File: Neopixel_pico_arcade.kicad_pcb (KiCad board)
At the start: 4 copper layers, 100 x 100 mm, 0 parts

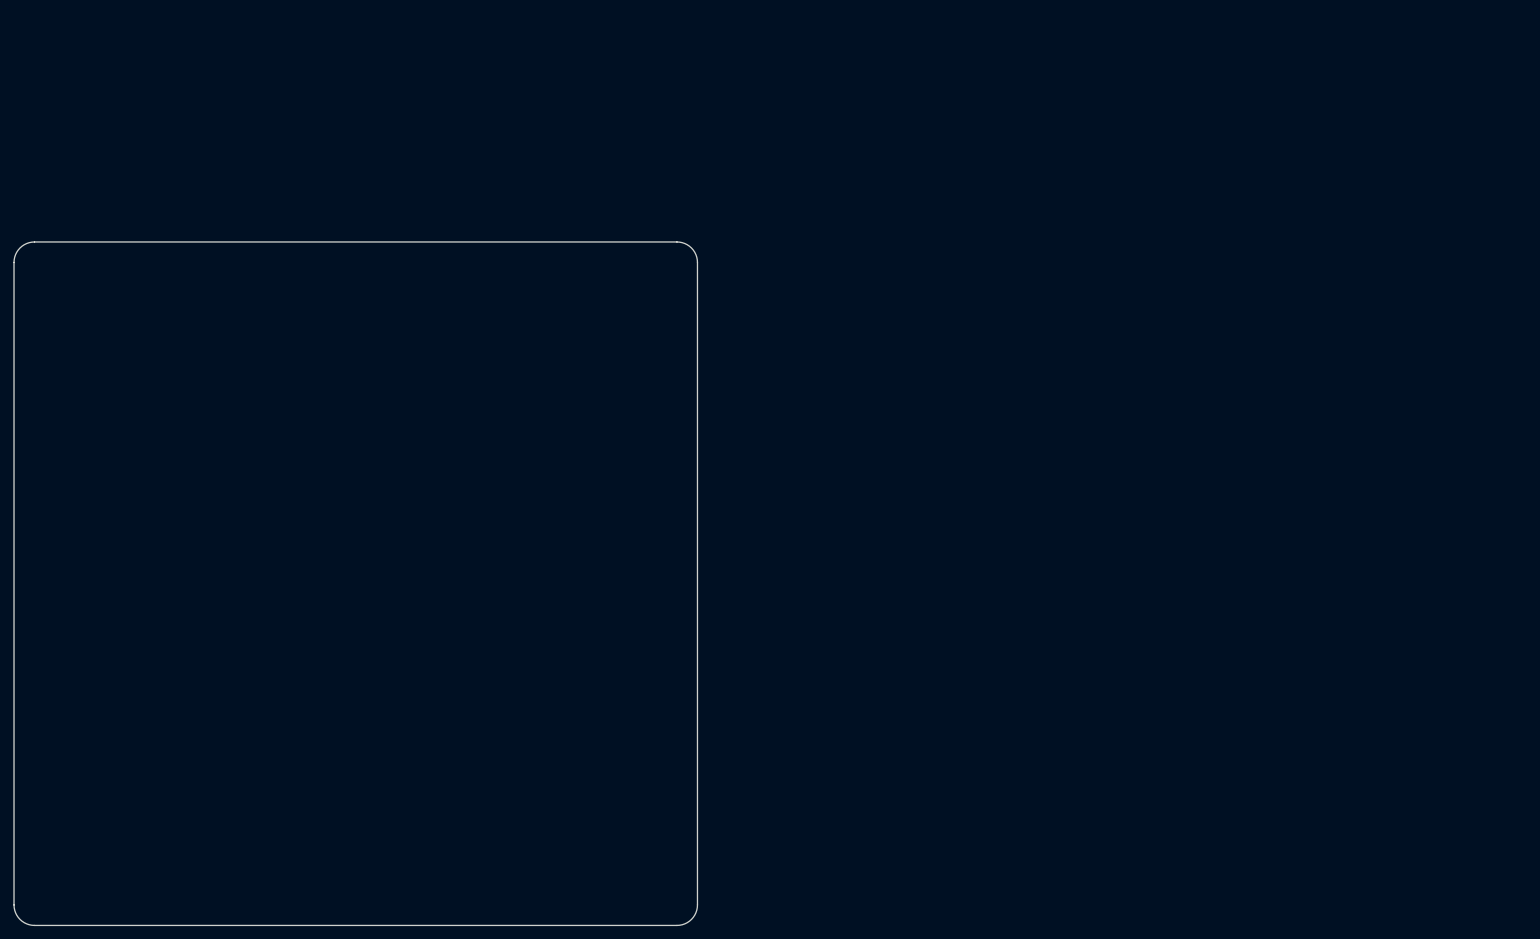
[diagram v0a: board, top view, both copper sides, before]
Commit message: Moves bottom side components roughly into place
The NES connector will still need to move to make space for the LEDs.
This probably means the PCB will need to grow.
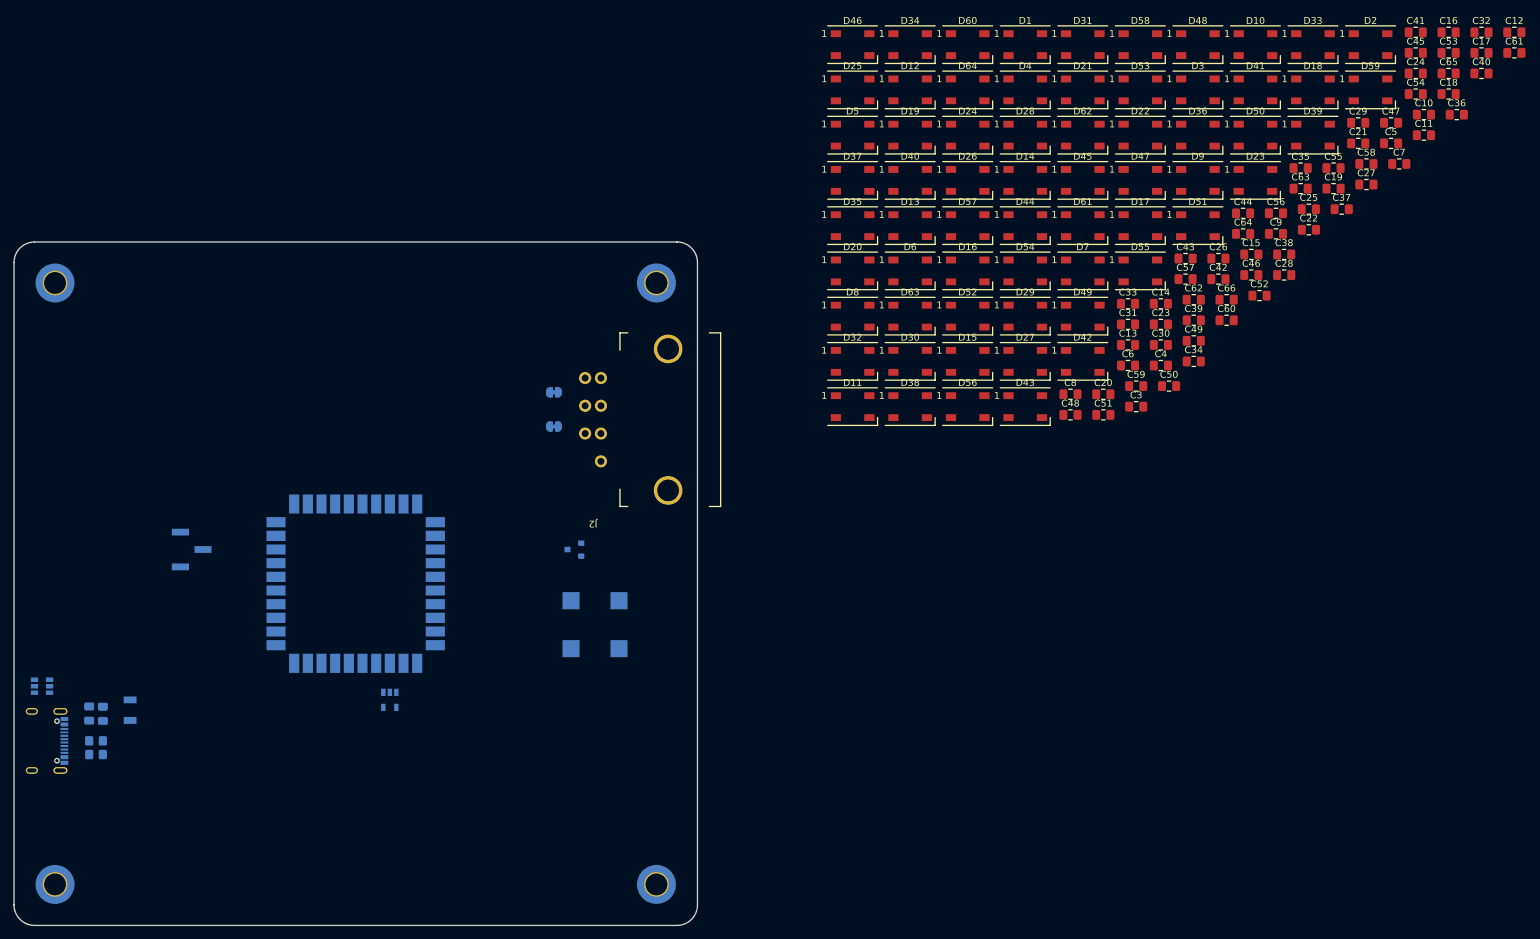
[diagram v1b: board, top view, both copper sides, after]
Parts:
- added BZ1: Buzzer, Buzzer_Beeper:MagneticBuzzer_CUI_CMT-8504-100-SMT, B.Cu at (185.0, 106.0)
- added C1: 4.7µF, Capacitor_SMD:C_0805_2012Metric_Pad1.18x1.45mm_HandSolder, B.Cu at (113.0, 119.0)
- added C10: 100nF, Capacitor_SMD:C_0805_2012Metric_Pad1.18x1.45mm_HandSolder, F.Cu at (306.3, 31.4)
- added C11: 100nF, Capacitor_SMD:C_0805_2012Metric_Pad1.18x1.45mm_HandSolder, F.Cu at (306.3, 34.4)
- added C12: 100nF, Capacitor_SMD:C_0805_2012Metric_Pad1.18x1.45mm_HandSolder, F.Cu at (319.5, 19.3)
- added C13: 100nF, Capacitor_SMD:C_0805_2012Metric_Pad1.18x1.45mm_HandSolder, F.Cu at (263.0, 65.1)
- added C14: 100nF, Capacitor_SMD:C_0805_2012Metric_Pad1.18x1.45mm_HandSolder, F.Cu at (267.8, 59.0)
- added C15: 100nF, Capacitor_SMD:C_0805_2012Metric_Pad1.18x1.45mm_HandSolder, F.Cu at (281.0, 51.8)
- added C16: 100nF, Capacitor_SMD:C_0805_2012Metric_Pad1.18x1.45mm_HandSolder, F.Cu at (309.9, 19.3)
- added C17: 100nF, Capacitor_SMD:C_0805_2012Metric_Pad1.18x1.45mm_HandSolder, F.Cu at (314.7, 22.3)
- added C18: 100nF, Capacitor_SMD:C_0805_2012Metric_Pad1.18x1.45mm_HandSolder, F.Cu at (309.9, 28.4)
- added C19: 100nF, Capacitor_SMD:C_0805_2012Metric_Pad1.18x1.45mm_HandSolder, F.Cu at (293.1, 42.2)
- added C2: 100nF, Capacitor_SMD:C_0805_2012Metric_Pad1.18x1.45mm_HandSolder, B.Cu at (111.0, 119.0)
- added C20: 100nF, Capacitor_SMD:C_0805_2012Metric_Pad1.18x1.45mm_HandSolder, F.Cu at (259.4, 72.3)
- added C21: 100nF, Capacitor_SMD:C_0805_2012Metric_Pad1.18x1.45mm_HandSolder, F.Cu at (296.7, 35.6)
- added C22: 100nF, Capacitor_SMD:C_0805_2012Metric_Pad1.18x1.45mm_HandSolder, F.Cu at (289.5, 48.2)
- added C23: 100nF, Capacitor_SMD:C_0805_2012Metric_Pad1.18x1.45mm_HandSolder, F.Cu at (267.8, 62.1)
- added C24: 100nF, Capacitor_SMD:C_0805_2012Metric_Pad1.18x1.45mm_HandSolder, F.Cu at (305.1, 25.3)
- added C25: 100nF, Capacitor_SMD:C_0805_2012Metric_Pad1.18x1.45mm_HandSolder, F.Cu at (289.5, 45.2)
- added C26: 100nF, Capacitor_SMD:C_0805_2012Metric_Pad1.18x1.45mm_HandSolder, F.Cu at (276.2, 52.4)
- added C27: 100nF, Capacitor_SMD:C_0805_2012Metric_Pad1.18x1.45mm_HandSolder, F.Cu at (297.9, 41.6)
- added C28: 100nF, Capacitor_SMD:C_0805_2012Metric_Pad1.18x1.45mm_HandSolder, F.Cu at (285.8, 54.8)
- added C29: 100nF, Capacitor_SMD:C_0805_2012Metric_Pad1.18x1.45mm_HandSolder, F.Cu at (296.7, 32.6)
- added C3: 100nF, Capacitor_SMD:C_0805_2012Metric_Pad1.18x1.45mm_HandSolder, F.Cu at (264.2, 74.1)
- added C30: 100nF, Capacitor_SMD:C_0805_2012Metric_Pad1.18x1.45mm_HandSolder, F.Cu at (267.8, 65.1)
- added C31: 100nF, Capacitor_SMD:C_0805_2012Metric_Pad1.18x1.45mm_HandSolder, F.Cu at (263.0, 62.1)
- added C32: 100nF, Capacitor_SMD:C_0805_2012Metric_Pad1.18x1.45mm_HandSolder, F.Cu at (314.7, 19.3)
- added C33: 100nF, Capacitor_SMD:C_0805_2012Metric_Pad1.18x1.45mm_HandSolder, F.Cu at (263.0, 59.0)
- added C34: 100nF, Capacitor_SMD:C_0805_2012Metric_Pad1.18x1.45mm_HandSolder, F.Cu at (272.6, 67.5)
- added C35: 100nF, Capacitor_SMD:C_0805_2012Metric_Pad1.18x1.45mm_HandSolder, F.Cu at (288.3, 39.2)
- added C36: 100nF, Capacitor_SMD:C_0805_2012Metric_Pad1.18x1.45mm_HandSolder, F.Cu at (311.1, 31.4)
- added C37: 100nF, Capacitor_SMD:C_0805_2012Metric_Pad1.18x1.45mm_HandSolder, F.Cu at (294.3, 45.2)
- added C38: 100nF, Capacitor_SMD:C_0805_2012Metric_Pad1.18x1.45mm_HandSolder, F.Cu at (285.8, 51.8)
- added C39: 100nF, Capacitor_SMD:C_0805_2012Metric_Pad1.18x1.45mm_HandSolder, F.Cu at (272.6, 61.5)
- added C4: 100nF, Capacitor_SMD:C_0805_2012Metric_Pad1.18x1.45mm_HandSolder, F.Cu at (267.8, 68.1)
- added C40: 100nF, Capacitor_SMD:C_0805_2012Metric_Pad1.18x1.45mm_HandSolder, F.Cu at (314.7, 25.3)
- added C41: 100nF, Capacitor_SMD:C_0805_2012Metric_Pad1.18x1.45mm_HandSolder, F.Cu at (305.1, 19.3)
- added C42: 100nF, Capacitor_SMD:C_0805_2012Metric_Pad1.18x1.45mm_HandSolder, F.Cu at (276.2, 55.4)
- added C43: 100nF, Capacitor_SMD:C_0805_2012Metric_Pad1.18x1.45mm_HandSolder, F.Cu at (271.4, 52.4)
- added C44: 100nF, Capacitor_SMD:C_0805_2012Metric_Pad1.18x1.45mm_HandSolder, F.Cu at (279.8, 45.8)
- added C45: 100nF, Capacitor_SMD:C_0805_2012Metric_Pad1.18x1.45mm_HandSolder, F.Cu at (305.1, 22.3)
- added C46: 100nF, Capacitor_SMD:C_0805_2012Metric_Pad1.18x1.45mm_HandSolder, F.Cu at (281.0, 54.8)
- added C47: 100nF, Capacitor_SMD:C_0805_2012Metric_Pad1.18x1.45mm_HandSolder, F.Cu at (301.5, 32.6)
- added C48: 100nF, Capacitor_SMD:C_0805_2012Metric_Pad1.18x1.45mm_HandSolder, F.Cu at (254.6, 75.3)
- added C49: 100nF, Capacitor_SMD:C_0805_2012Metric_Pad1.18x1.45mm_HandSolder, F.Cu at (272.6, 64.5)
- added C5: 100nF, Capacitor_SMD:C_0805_2012Metric_Pad1.18x1.45mm_HandSolder, F.Cu at (301.5, 35.6)
- added C50: 100nF, Capacitor_SMD:C_0805_2012Metric_Pad1.18x1.45mm_HandSolder, F.Cu at (269.0, 71.1)
- added C51: 100nF, Capacitor_SMD:C_0805_2012Metric_Pad1.18x1.45mm_HandSolder, F.Cu at (259.4, 75.3)
- added C52: 100nF, Capacitor_SMD:C_0805_2012Metric_Pad1.18x1.45mm_HandSolder, F.Cu at (282.2, 57.8)
- added C53: 100nF, Capacitor_SMD:C_0805_2012Metric_Pad1.18x1.45mm_HandSolder, F.Cu at (309.9, 22.3)
- added C54: 100nF, Capacitor_SMD:C_0805_2012Metric_Pad1.18x1.45mm_HandSolder, F.Cu at (305.1, 28.4)
- added C55: 100nF, Capacitor_SMD:C_0805_2012Metric_Pad1.18x1.45mm_HandSolder, F.Cu at (293.1, 39.2)
- added C56: 100nF, Capacitor_SMD:C_0805_2012Metric_Pad1.18x1.45mm_HandSolder, F.Cu at (284.6, 45.8)
- added C57: 100nF, Capacitor_SMD:C_0805_2012Metric_Pad1.18x1.45mm_HandSolder, F.Cu at (271.4, 55.4)
- added C58: 100nF, Capacitor_SMD:C_0805_2012Metric_Pad1.18x1.45mm_HandSolder, F.Cu at (297.9, 38.6)
- added C59: 100nF, Capacitor_SMD:C_0805_2012Metric_Pad1.18x1.45mm_HandSolder, F.Cu at (264.2, 71.1)
- added C6: 100nF, Capacitor_SMD:C_0805_2012Metric_Pad1.18x1.45mm_HandSolder, F.Cu at (263.0, 68.1)
- added C60: 100nF, Capacitor_SMD:C_0805_2012Metric_Pad1.18x1.45mm_HandSolder, F.Cu at (277.4, 61.5)
- added C61: 100nF, Capacitor_SMD:C_0805_2012Metric_Pad1.18x1.45mm_HandSolder, F.Cu at (319.5, 22.3)
- added C62: 100nF, Capacitor_SMD:C_0805_2012Metric_Pad1.18x1.45mm_HandSolder, F.Cu at (272.6, 58.4)
- added C63: 100nF, Capacitor_SMD:C_0805_2012Metric_Pad1.18x1.45mm_HandSolder, F.Cu at (288.3, 42.2)
- added C64: 100nF, Capacitor_SMD:C_0805_2012Metric_Pad1.18x1.45mm_HandSolder, F.Cu at (279.8, 48.8)
- added C65: 100nF, Capacitor_SMD:C_0805_2012Metric_Pad1.18x1.45mm_HandSolder, F.Cu at (309.9, 25.3)
- added C66: 100nF, Capacitor_SMD:C_0805_2012Metric_Pad1.18x1.45mm_HandSolder, F.Cu at (277.4, 58.4)
- added C7: 100nF, Capacitor_SMD:C_0805_2012Metric_Pad1.18x1.45mm_HandSolder, F.Cu at (302.7, 38.6)
- added C8: 100nF, Capacitor_SMD:C_0805_2012Metric_Pad1.18x1.45mm_HandSolder, F.Cu at (254.6, 72.3)
- added C9: 100nF, Capacitor_SMD:C_0805_2012Metric_Pad1.18x1.45mm_HandSolder, F.Cu at (284.6, 48.8)
- added D1: WS2812C, LED_SMD:LED_WS2812B_PLCC4_5.0x5.0mm_P3.2mm, F.Cu at (248.0, 21.1)
- added D10: WS2812C, LED_SMD:LED_WS2812B_PLCC4_5.0x5.0mm_P3.2mm, F.Cu at (281.6, 21.1)
- added D11: WS2812C, LED_SMD:LED_WS2812B_PLCC4_5.0x5.0mm_P3.2mm, F.Cu at (222.7, 74.1)
- added D12: WS2812C, LED_SMD:LED_WS2812B_PLCC4_5.0x5.0mm_P3.2mm, F.Cu at (231.1, 27.8)
- added D13: WS2812C, LED_SMD:LED_WS2812B_PLCC4_5.0x5.0mm_P3.2mm, F.Cu at (231.1, 47.6)
- added D14: WS2812C, LED_SMD:LED_WS2812B_PLCC4_5.0x5.0mm_P3.2mm, F.Cu at (248.0, 41.0)
- added D15: WS2812C, LED_SMD:LED_WS2812B_PLCC4_5.0x5.0mm_P3.2mm, F.Cu at (239.5, 67.5)
- added D16: WS2812C, LED_SMD:LED_WS2812B_PLCC4_5.0x5.0mm_P3.2mm, F.Cu at (239.5, 54.2)
- added D17: WS2812C, LED_SMD:LED_WS2812B_PLCC4_5.0x5.0mm_P3.2mm, F.Cu at (264.8, 47.6)
- added D18: WS2812C, LED_SMD:LED_WS2812B_PLCC4_5.0x5.0mm_P3.2mm, F.Cu at (290.1, 27.8)
- added D19: WS2812C, LED_SMD:LED_WS2812B_PLCC4_5.0x5.0mm_P3.2mm, F.Cu at (231.1, 34.4)
- added D2: WS2812C, LED_SMD:LED_WS2812B_PLCC4_5.0x5.0mm_P3.2mm, F.Cu at (298.5, 21.1)
- added D20: WS2812C, LED_SMD:LED_WS2812B_PLCC4_5.0x5.0mm_P3.2mm, F.Cu at (222.7, 54.2)
- added D21: WS2812C, LED_SMD:LED_WS2812B_PLCC4_5.0x5.0mm_P3.2mm, F.Cu at (256.4, 27.8)
- added D22: WS2812C, LED_SMD:LED_WS2812B_PLCC4_5.0x5.0mm_P3.2mm, F.Cu at (264.8, 34.4)
- added D23: WS2812C, LED_SMD:LED_WS2812B_PLCC4_5.0x5.0mm_P3.2mm, F.Cu at (281.6, 41.0)
- added D24: WS2812C, LED_SMD:LED_WS2812B_PLCC4_5.0x5.0mm_P3.2mm, F.Cu at (239.5, 34.4)
- added D25: WS2812C, LED_SMD:LED_WS2812B_PLCC4_5.0x5.0mm_P3.2mm, F.Cu at (222.7, 27.8)
- added D26: WS2812C, LED_SMD:LED_WS2812B_PLCC4_5.0x5.0mm_P3.2mm, F.Cu at (239.5, 41.0)
- added D27: WS2812C, LED_SMD:LED_WS2812B_PLCC4_5.0x5.0mm_P3.2mm, F.Cu at (248.0, 67.5)
- added D28: WS2812C, LED_SMD:LED_WS2812B_PLCC4_5.0x5.0mm_P3.2mm, F.Cu at (248.0, 34.4)
- added D29: WS2812C, LED_SMD:LED_WS2812B_PLCC4_5.0x5.0mm_P3.2mm, F.Cu at (248.0, 60.9)
- added D3: WS2812C, LED_SMD:LED_WS2812B_PLCC4_5.0x5.0mm_P3.2mm, F.Cu at (273.2, 27.8)
- added D30: WS2812C, LED_SMD:LED_WS2812B_PLCC4_5.0x5.0mm_P3.2mm, F.Cu at (231.1, 67.5)
- added D31: WS2812C, LED_SMD:LED_WS2812B_PLCC4_5.0x5.0mm_P3.2mm, F.Cu at (256.4, 21.1)
- added D32: WS2812C, LED_SMD:LED_WS2812B_PLCC4_5.0x5.0mm_P3.2mm, F.Cu at (222.7, 67.5)
- added D33: WS2812C, LED_SMD:LED_WS2812B_PLCC4_5.0x5.0mm_P3.2mm, F.Cu at (290.1, 21.1)
- added D34: WS2812C, LED_SMD:LED_WS2812B_PLCC4_5.0x5.0mm_P3.2mm, F.Cu at (231.1, 21.1)
- added D35: WS2812C, LED_SMD:LED_WS2812B_PLCC4_5.0x5.0mm_P3.2mm, F.Cu at (222.7, 47.6)
- added D36: WS2812C, LED_SMD:LED_WS2812B_PLCC4_5.0x5.0mm_P3.2mm, F.Cu at (273.2, 34.4)
- added D37: WS2812C, LED_SMD:LED_WS2812B_PLCC4_5.0x5.0mm_P3.2mm, F.Cu at (222.7, 41.0)
- added D38: WS2812C, LED_SMD:LED_WS2812B_PLCC4_5.0x5.0mm_P3.2mm, F.Cu at (231.1, 74.1)
- added D39: WS2812C, LED_SMD:LED_WS2812B_PLCC4_5.0x5.0mm_P3.2mm, F.Cu at (290.1, 34.4)
- added D4: WS2812C, LED_SMD:LED_WS2812B_PLCC4_5.0x5.0mm_P3.2mm, F.Cu at (248.0, 27.8)
- added D40: WS2812C, LED_SMD:LED_WS2812B_PLCC4_5.0x5.0mm_P3.2mm, F.Cu at (231.1, 41.0)
- added D41: WS2812C, LED_SMD:LED_WS2812B_PLCC4_5.0x5.0mm_P3.2mm, F.Cu at (281.6, 27.8)
- added D42: WS2812C, LED_SMD:LED_WS2812B_PLCC4_5.0x5.0mm_P3.2mm, F.Cu at (256.4, 67.5)
- added D43: WS2812C, LED_SMD:LED_WS2812B_PLCC4_5.0x5.0mm_P3.2mm, F.Cu at (248.0, 74.1)
- added D44: WS2812C, LED_SMD:LED_WS2812B_PLCC4_5.0x5.0mm_P3.2mm, F.Cu at (248.0, 47.6)
- added D45: WS2812C, LED_SMD:LED_WS2812B_PLCC4_5.0x5.0mm_P3.2mm, F.Cu at (256.4, 41.0)
- added D46: WS2812C, LED_SMD:LED_WS2812B_PLCC4_5.0x5.0mm_P3.2mm, F.Cu at (222.7, 21.1)
- added D47: WS2812C, LED_SMD:LED_WS2812B_PLCC4_5.0x5.0mm_P3.2mm, F.Cu at (264.8, 41.0)
- added D48: WS2812C, LED_SMD:LED_WS2812B_PLCC4_5.0x5.0mm_P3.2mm, F.Cu at (273.2, 21.1)
- added D49: WS2812C, LED_SMD:LED_WS2812B_PLCC4_5.0x5.0mm_P3.2mm, F.Cu at (256.4, 60.9)
- added D5: WS2812C, LED_SMD:LED_WS2812B_PLCC4_5.0x5.0mm_P3.2mm, F.Cu at (222.7, 34.4)
- added D50: WS2812C, LED_SMD:LED_WS2812B_PLCC4_5.0x5.0mm_P3.2mm, F.Cu at (281.6, 34.4)
- added D51: WS2812C, LED_SMD:LED_WS2812B_PLCC4_5.0x5.0mm_P3.2mm, F.Cu at (273.2, 47.6)
- added D52: WS2812C, LED_SMD:LED_WS2812B_PLCC4_5.0x5.0mm_P3.2mm, F.Cu at (239.5, 60.9)
- added D53: WS2812C, LED_SMD:LED_WS2812B_PLCC4_5.0x5.0mm_P3.2mm, F.Cu at (264.8, 27.8)
- added D54: WS2812C, LED_SMD:LED_WS2812B_PLCC4_5.0x5.0mm_P3.2mm, F.Cu at (248.0, 54.2)
- added D55: WS2812C, LED_SMD:LED_WS2812B_PLCC4_5.0x5.0mm_P3.2mm, F.Cu at (264.8, 54.2)
- added D56: WS2812C, LED_SMD:LED_WS2812B_PLCC4_5.0x5.0mm_P3.2mm, F.Cu at (239.5, 74.1)
- added D57: WS2812C, LED_SMD:LED_WS2812B_PLCC4_5.0x5.0mm_P3.2mm, F.Cu at (239.5, 47.6)
- added D58: WS2812C, LED_SMD:LED_WS2812B_PLCC4_5.0x5.0mm_P3.2mm, F.Cu at (264.8, 21.1)
- added D59: WS2812C, LED_SMD:LED_WS2812B_PLCC4_5.0x5.0mm_P3.2mm, F.Cu at (298.5, 27.8)
- added D6: WS2812C, LED_SMD:LED_WS2812B_PLCC4_5.0x5.0mm_P3.2mm, F.Cu at (231.1, 54.2)
- added D60: WS2812C, LED_SMD:LED_WS2812B_PLCC4_5.0x5.0mm_P3.2mm, F.Cu at (239.5, 21.1)
- added D61: WS2812C, LED_SMD:LED_WS2812B_PLCC4_5.0x5.0mm_P3.2mm, F.Cu at (256.4, 47.6)
- added D62: WS2812C, LED_SMD:LED_WS2812B_PLCC4_5.0x5.0mm_P3.2mm, F.Cu at (256.4, 34.4)
- added D63: WS2812C, LED_SMD:LED_WS2812B_PLCC4_5.0x5.0mm_P3.2mm, F.Cu at (231.1, 60.9)
- added D64: WS2812C, LED_SMD:LED_WS2812B_PLCC4_5.0x5.0mm_P3.2mm, F.Cu at (239.5, 27.8)
- added D7: WS2812C, LED_SMD:LED_WS2812B_PLCC4_5.0x5.0mm_P3.2mm, F.Cu at (256.4, 54.2)
- added D8: WS2812C, LED_SMD:LED_WS2812B_PLCC4_5.0x5.0mm_P3.2mm, F.Cu at (222.7, 60.9)
- added D9: WS2812C, LED_SMD:LED_WS2812B_PLCC4_5.0x5.0mm_P3.2mm, F.Cu at (273.2, 41.0)
- added F1: PTC 1A, Neopixel_pico_arcade:Belfuse_0ZCJ, B.Cu at (117.0, 118.5)
- added H1: MountingHole_Pad, MountingHole:MountingHole_3.2mm_M3_ISO7380_Pad_TopOnly, B.Cu at (194.0, 56.0)
- added H2: MountingHole_Pad, MountingHole:MountingHole_3.2mm_M3_ISO7380_Pad_TopOnly, B.Cu at (106.0, 56.0)
- added H3: MountingHole_Pad, MountingHole:MountingHole_3.2mm_M3_ISO7380_Pad_TopOnly, B.Cu at (194.0, 144.0)
- added H4: MountingHole_Pad, MountingHole:MountingHole_3.2mm_M3_ISO7380_Pad_TopOnly, B.Cu at (106.0, 144.0)
- added J1: SWD_connector, Connector_PinHeader_2.54mm:PinHeader_1x03_P2.54mm_Vertical_SMD_Pin1Left, B.Cu at (126.0, 95.0)
- added J2: NES_controller_connector, Neopixel_pico_arcade:NES_Controller_connector, F.Cu at (184.7, 76.0)
- added J3: USB_C_Receptacle_USB2.0, Neopixel_pico_arcade:USB_C_Receptacle_USB_2_GTC_USB4105, B.Cu at (105.0, 123.0)
- added JP1: jmp, Jumper:SolderJumper-2_P1.3mm_Bridged_RoundedPad1.0x1.5mm, B.Cu at (179.0, 77.0)
- added JP2: jmp, Jumper:SolderJumper-2_P1.3mm_Bridged_RoundedPad1.0x1.5mm, B.Cu at (179.0, 72.0)
- added Q1: 2N7002, Package_TO_SOT_SMD:SOT-23, B.Cu at (182.0, 95.0)
- added R1: 5.1kΩ, Resistor_SMD:R_0805_2012Metric_Pad1.20x1.40mm_HandSolder, B.Cu at (112.0, 125.0)
- added R2: 5.1kΩ, Resistor_SMD:R_0805_2012Metric_Pad1.20x1.40mm_HandSolder, B.Cu at (112.0, 123.0)
- added U1: RP2040_Stamp, RP2040_stamp:RP2040_Stamp_SMD, B.Cu at (150.0, 100.0)
- added U2: SN74LV1T34DBV, Package_TO_SOT_SMD:SOT-23-5, B.Cu at (155.0, 117.0)
- added U3: SRV05-4HTG-D, Package_TO_SOT_SMD:SOT-23-6, B.Cu at (104.1, 115.0)

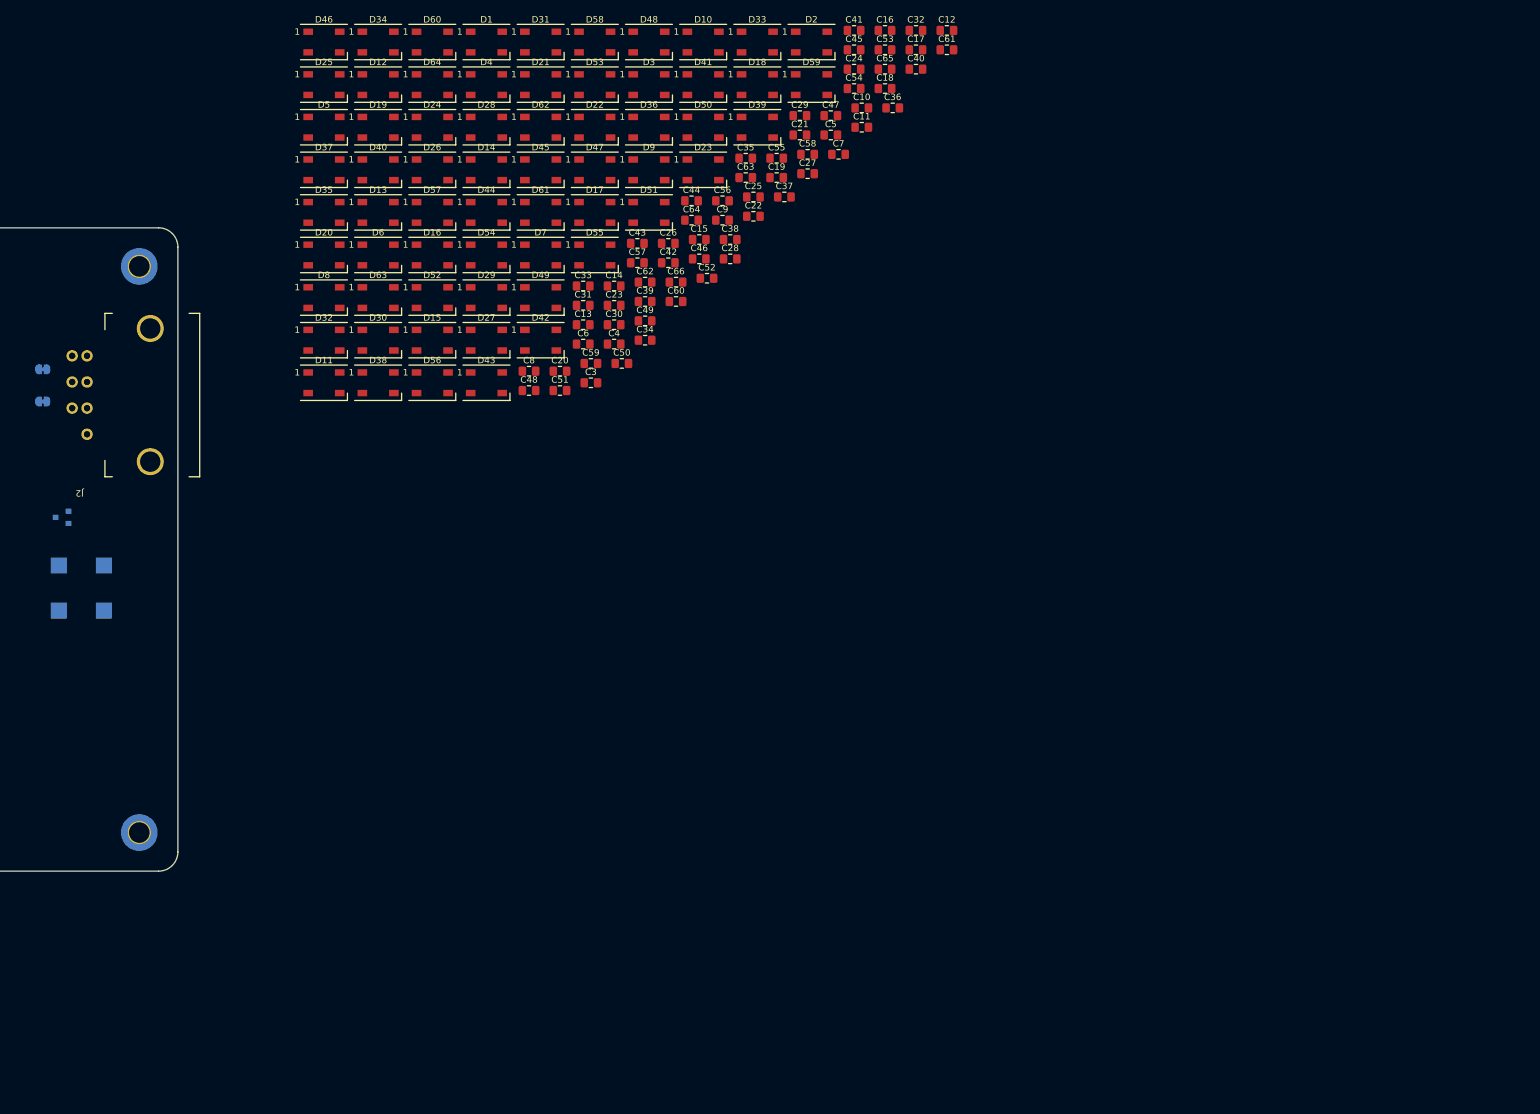
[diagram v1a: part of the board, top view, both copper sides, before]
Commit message: Arranges LEDs in an ordered matrix
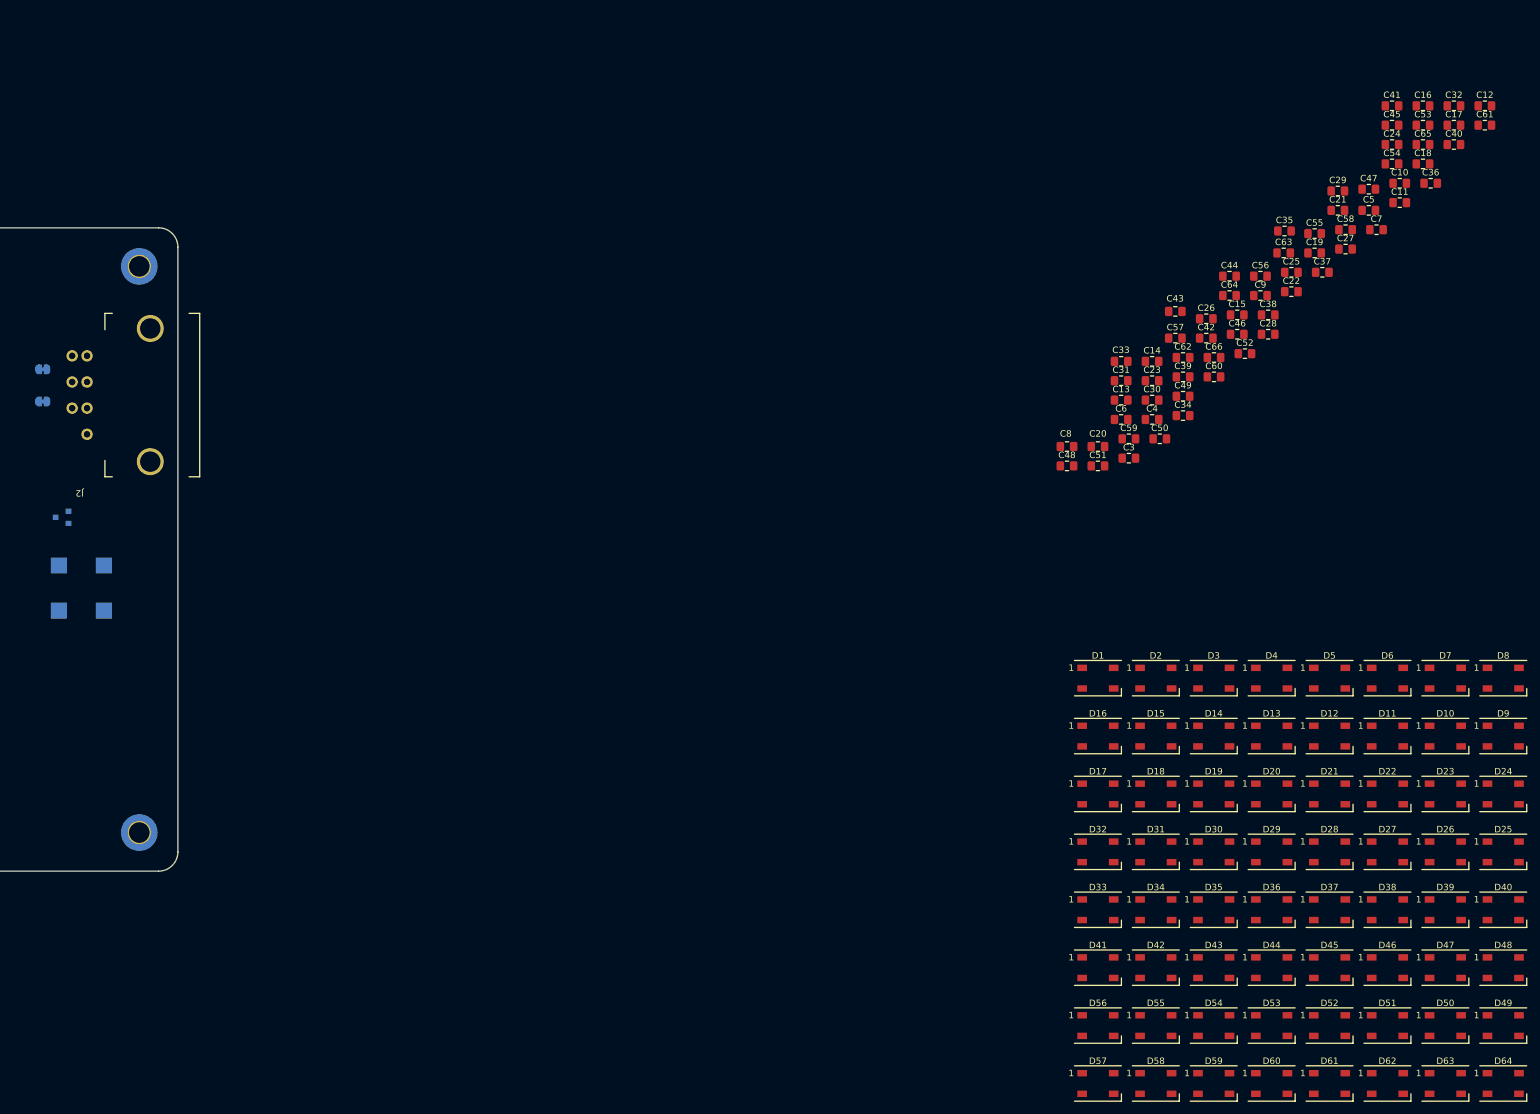
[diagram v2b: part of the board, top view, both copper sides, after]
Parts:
- moved D64 227.6 mm to (406.0, 183.0)
- moved D46 219.1 mm to (388.0, 165.0)
- moved D25 218.7 mm to (406.0, 147.0)
- moved D40 209.3 mm to (406.0, 156.0)
- moved D60 207.9 mm to (370.0, 183.0)
- moved D63 206.0 mm to (397.0, 183.0)
- moved D62 198.5 mm to (388.0, 183.0)
- moved D24 196.1 mm to (406.0, 138.0)
- moved D48 195.8 mm to (406.0, 165.0)
- moved D37 194.1 mm to (379.0, 156.0)
- moved D8 192.6 mm to (406.0, 120.0)
- moved D26 189.8 mm to (397.0, 147.0)
- moved D49 187.6 mm to (406.0, 174.0)
- moved D58 183.9 mm to (352.0, 183.0)
- moved D61 182.7 mm to (379.0, 183.0)
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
